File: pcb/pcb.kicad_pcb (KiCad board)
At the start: 2 copper layers, 65 x 56 mm, 298 parts, among them J1 Conn_02x20_Odd_Even

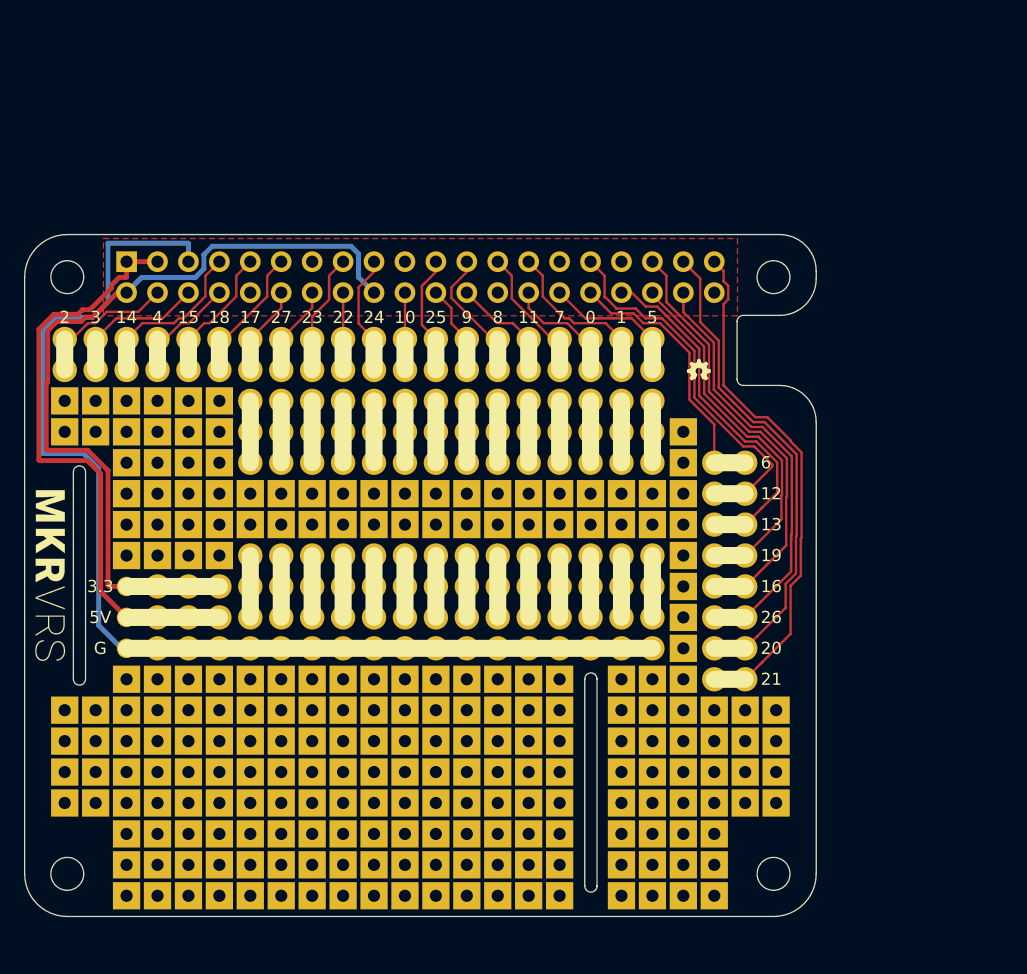
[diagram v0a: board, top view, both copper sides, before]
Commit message: v20 fix GPIO21 short to ground
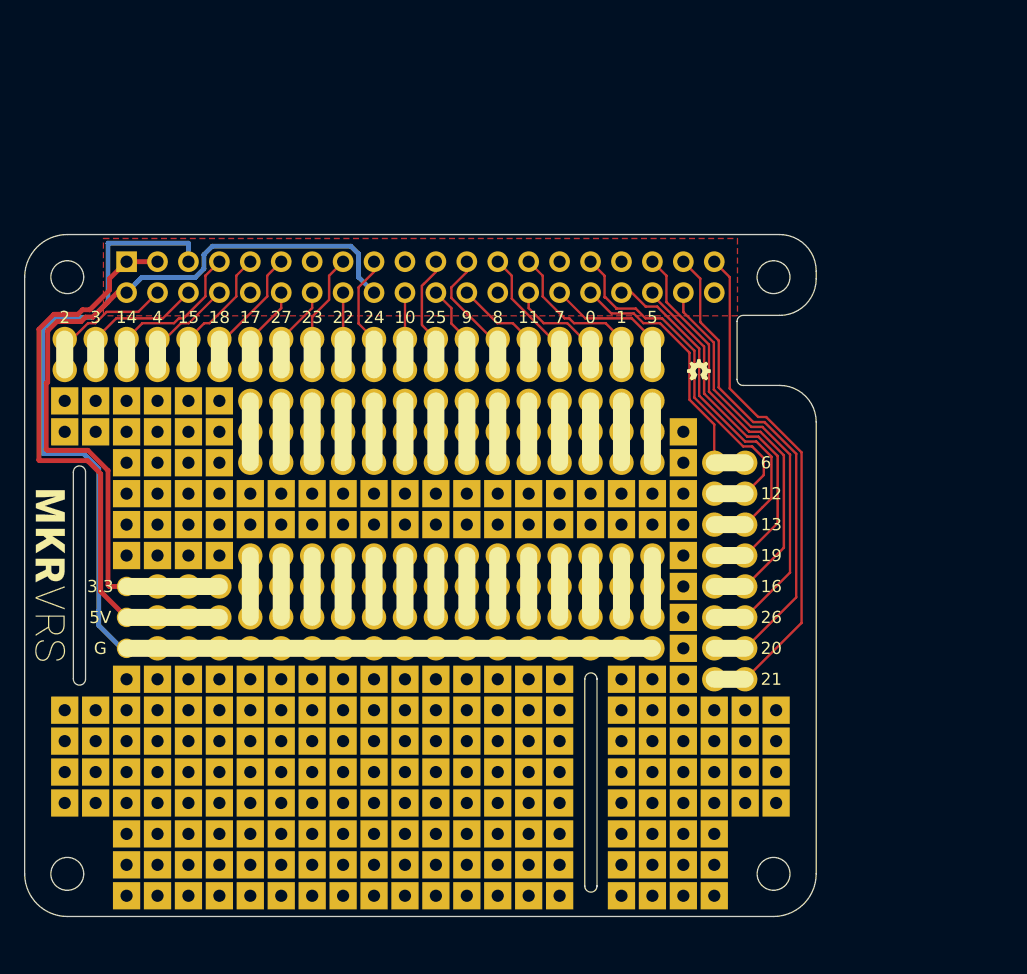
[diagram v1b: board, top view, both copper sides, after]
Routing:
- net /GPIO21: track 40.3 -> 39.6 mm
- net /GPIO12: track 28.5 -> 27.8 mm
- net /GPIO26: track 33.0 -> 32.4 mm
- net /GPIO13: track 27.2 -> 26.6 mm
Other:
- net class Default removed
- board text added: "Designed at Core Electronics by Brenton Schulz and Michael Ruppe"

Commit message: got schematic for eeprom in; no layout
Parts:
- added JP1: SolderJumper_2_Bridged, Jumper:SolderJumper-2_P1.3mm_Bridged_RoundedPad1.0x1.5mm, F.Cu at (176.8, 80.6)
- added R1: 3K9, Resistor_SMD:R_0603_1608Metric_Pad0.98x0.95mm_HandSolder, F.Cu at (160.9, 82.1)
- added R2: 3K9, Resistor_SMD:R_0603_1608Metric_Pad0.98x0.95mm_HandSolder, F.Cu at (153.3, 77.1)
- added R3: 3K9, Resistor_SMD:R_0603_1608Metric_Pad0.98x0.95mm_HandSolder, F.Cu at (153.3, 79.6)
- added U1: CAT24C32, Package_SO:SOIC-8_3.9x4.9mm_P1.27mm, F.Cu at (163.5, 76.7)
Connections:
- net /GPIO0 renamed /EEDATA
- net /GPIO1 renamed /EECLK

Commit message: something
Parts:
- removed the REF** at (156.0, 131.2)
- removed the REF** at (158.5, 131.2)
- removed the REF** at (166.1, 131.2)
- removed the REF** at (163.6, 131.2)
- removed the REF** at (161.0, 133.7)
- removed the REF** at (161.0, 136.2)
- added REF**: SquarePad-2.24mm-0.3mm-Back-0.5mm-Front-clearance, lib:SquarePad-2.24mm-0.3mm-Back-0.5mm-Front-clearance, F.Cu at (161.0, 133.7)
- added REF**: SquarePad-2.24mm-0.3mm-Back-0.5mm-Front-clearance, lib:SquarePad-2.24mm-0.3mm-Back-0.5mm-Front-clearance, F.Cu at (156.0, 131.1)
- added REF**: SquarePad-2.24mm-0.3mm-Back-0.5mm-Front-clearance, lib:SquarePad-2.24mm-0.3mm-Back-0.5mm-Front-clearance, F.Cu at (163.6, 131.1)
- added REF**: SquarePad-2.24mm-0.3mm-Back-0.5mm-Front-clearance, lib:SquarePad-2.24mm-0.3mm-Back-0.5mm-Front-clearance, F.Cu at (161.0, 136.3)
- added REF**: SquarePad-2.24mm-0.3mm-Back-0.5mm-Front-clearance, lib:SquarePad-2.24mm-0.3mm-Back-0.5mm-Front-clearance, F.Cu at (166.1, 131.1)
- added REF**: SquarePad-2.24mm-0.3mm-Back-0.5mm-Front-clearance, lib:SquarePad-2.24mm-0.3mm-Back-0.5mm-Front-clearance, F.Cu at (158.5, 131.1)
- moved R2 72.7 mm to (177.2, 145.8), turned to 90 degrees
- moved R3 70.9 mm to (178.8, 145.8), turned to 90 degrees
- moved R1 66.6 mm to (180.3, 145.8), turned to 90 degrees
- moved U1 65.5 mm to (179.9, 140.1), turned to -90 degrees
- moved JP1 65.4 mm to (182.6, 145.8), turned to -90 degrees
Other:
- board text added: "Designed at Core Electronics by Brenton Schulz and Michael Ruppe updated by mtfurlan"
- board text removed: "Designed at Core Electronics by Brenton Schulz and Michael Ruppe"
